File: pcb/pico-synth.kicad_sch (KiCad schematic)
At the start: 48 parts, among them J1 JST XH 2P, J2 JST XH 5P, J3 JST XH 4P, J4 JST XH 3P, SW1 Rotary_Encoder_Switch, U1 Pico, U2 6N137, U3 24LC512, U4 MCP4822, U5 LTC1044, U6 TL071, U7 TL072

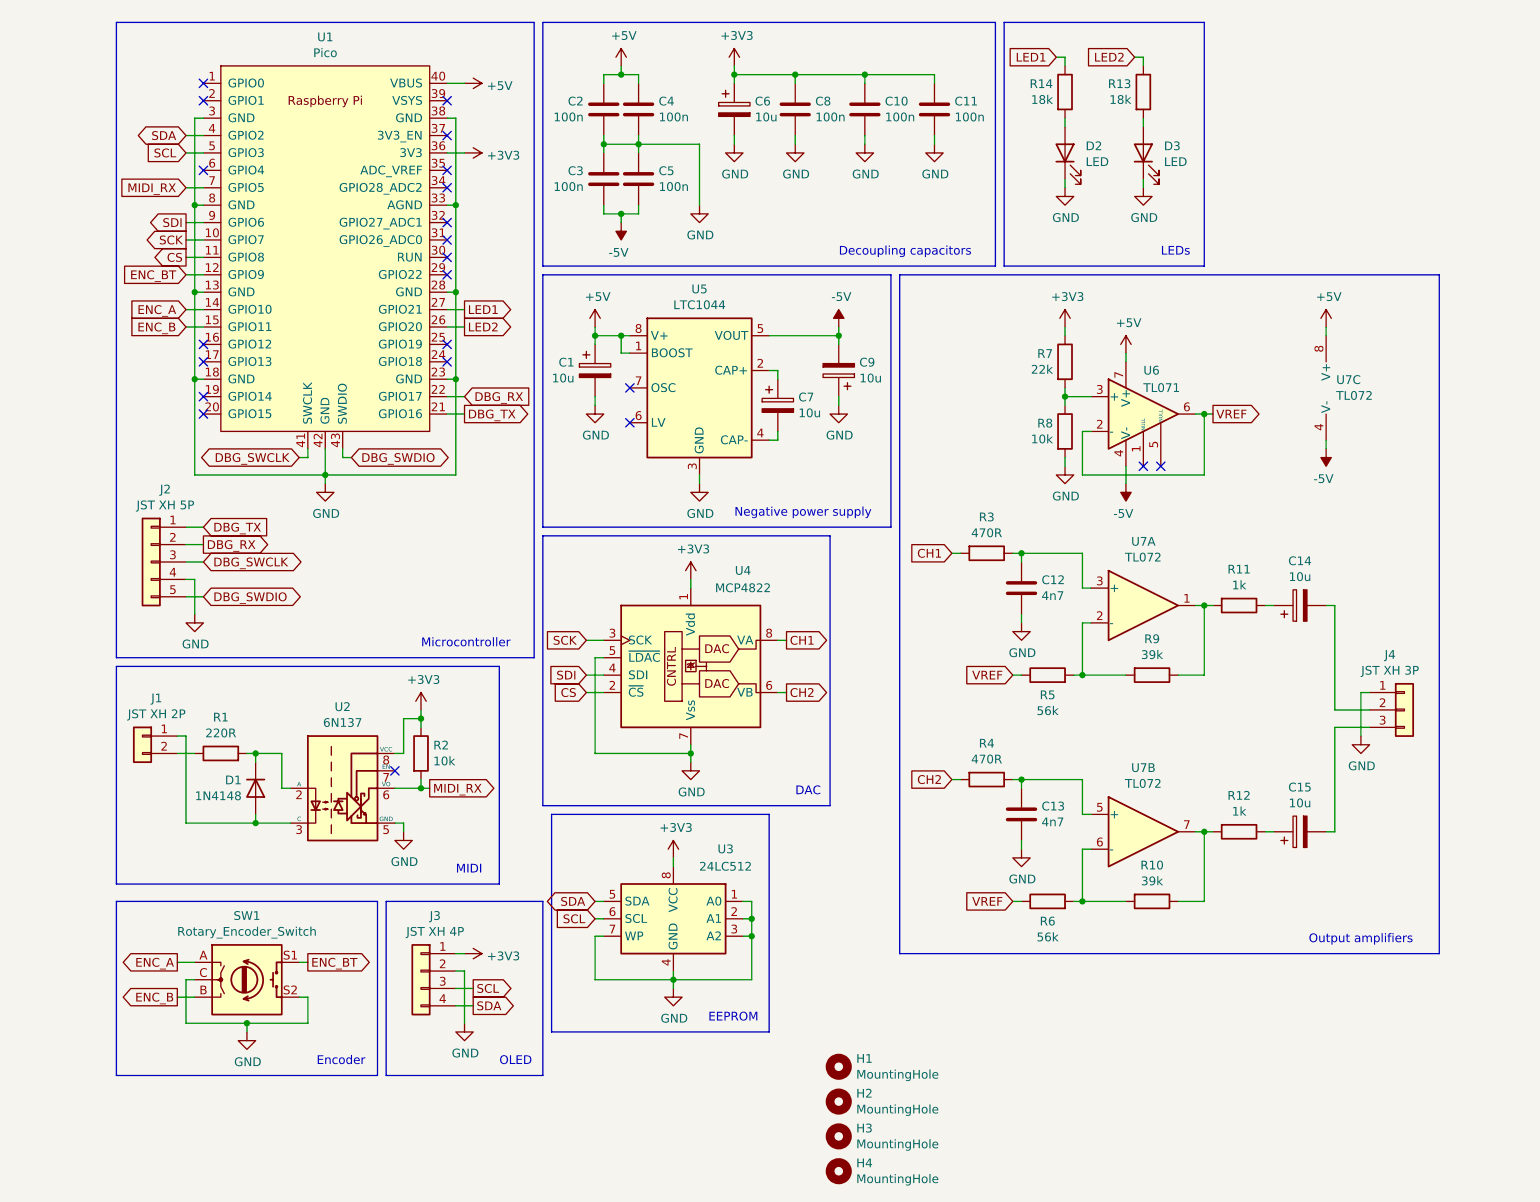
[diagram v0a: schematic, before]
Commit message: new hardware revision: 3.0
- added better output filter (Sallen-Key low pass filter)
- use MCP4822's LDAC pin to avoid (minimal, negligible :) phase drift
  between the channels
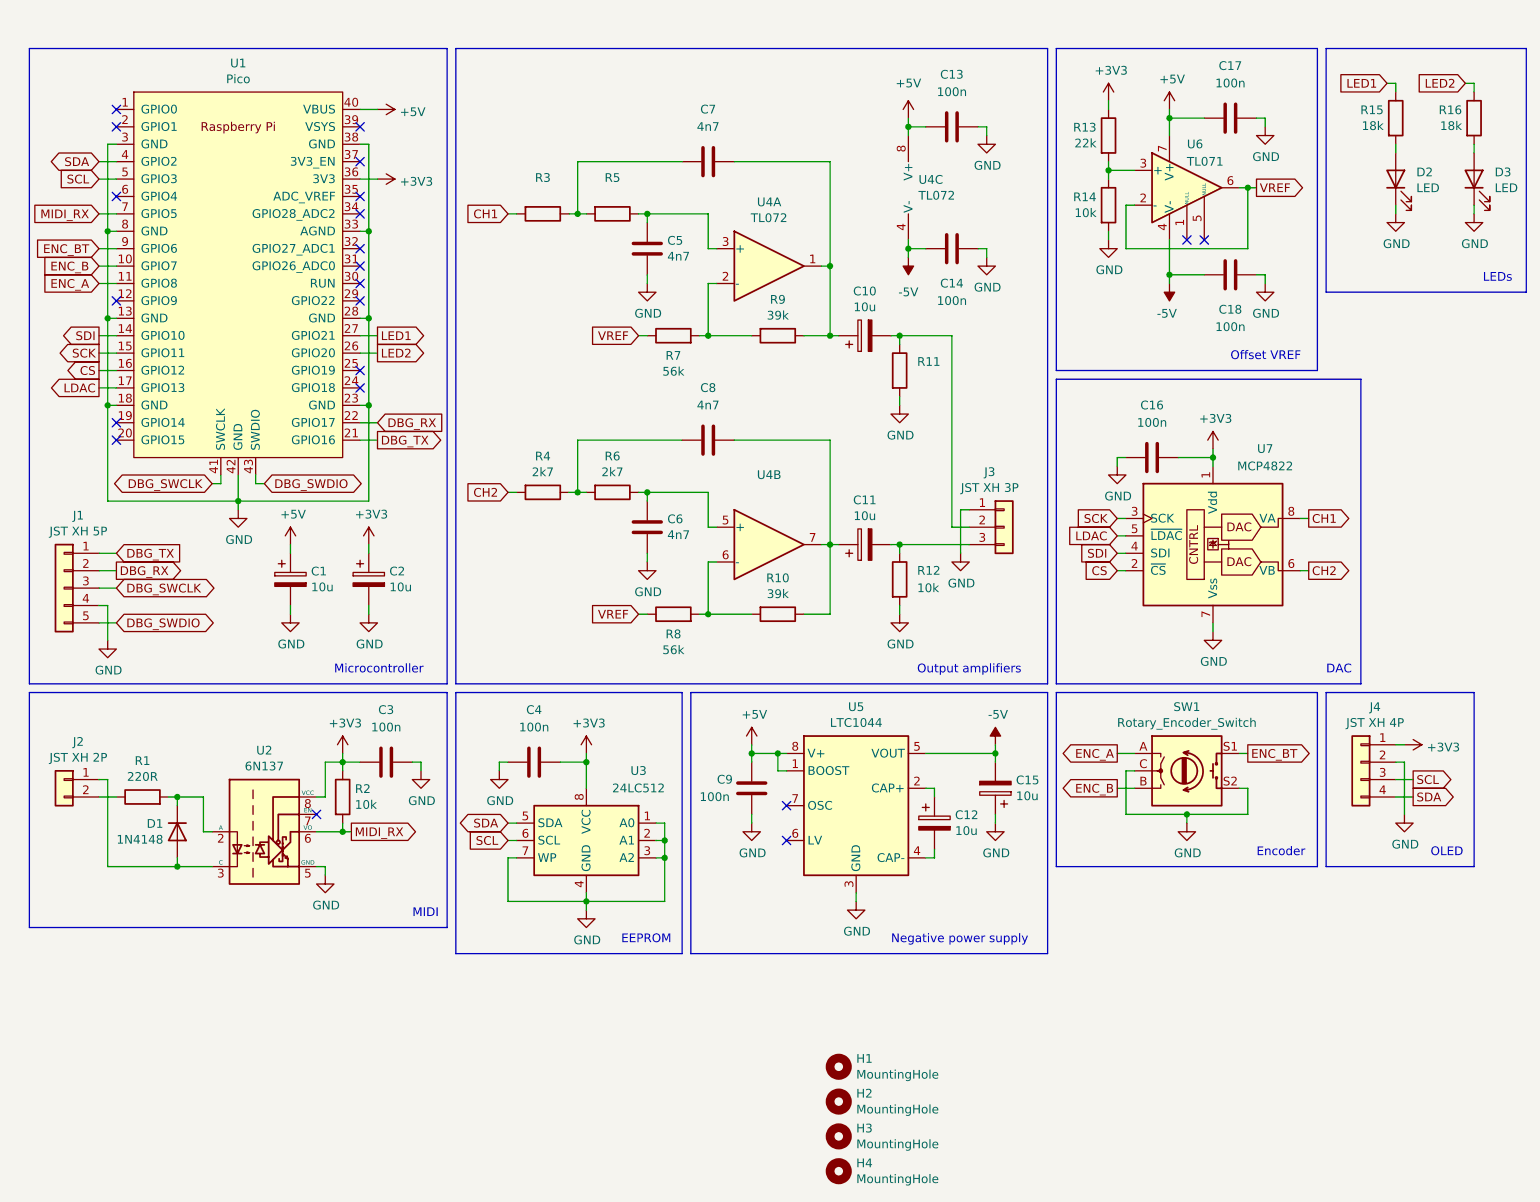
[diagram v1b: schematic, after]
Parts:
- removed C10, C11, C2, C5: 100n, Capacitor_THT:C_Disc_D4.3mm_W1.9mm_P5.00mm, symbol Device:C
- removed C15, C6: 10u, Capacitor_THT:CP_Radial_D5.0mm_P2.50mm, symbol Device:C_Polarized
- removed unit 2 of U7
- added C11, C2: 10u, Capacitor_THT:CP_Radial_D5.0mm_P2.50mm, symbol Device:C_Polarized
- added C14, C16, C17, C18, C9: 100n, Capacitor_THT:C_Disc_D4.3mm_W1.9mm_P5.00mm, symbol Device:C
- added C6, C7: 4n7, symbol Device:C
- added R3: (no value), Resistor_THT:R_Axial_DIN0207_L6.3mm_D2.5mm_P10.16mm_Horizontal, symbol Device:R
- added R8: 56k, Resistor_THT:R_Axial_DIN0207_L6.3mm_D2.5mm_P10.16mm_Horizontal, symbol Device:R
- added unit 2 of U4
- C13: value 4n7 -> 100n; footprint Capacitor_THT:C_Disc_D3.0mm_W1.6mm_P2.50mm -> Capacitor_THT:C_Disc_D4.3mm_W1.9mm_P5.00mm
- C5: renamed from C12; footprint Capacitor_THT:C_Disc_D3.0mm_W1.6mm_P2.50mm -> (none)
- C8: value 100n -> 4n7; footprint Capacitor_THT:C_Disc_D4.3mm_W1.9mm_P5.00mm -> (none)
- R11: value 1k -> (none)
- R12: value 1k -> 10k
- R4: value 470R -> 2k7
- R5: renamed from R3; value 470R -> (none)
- R6: value 56k -> 2k7
- U2: footprint (none) -> Package_DIP:DIP-8_W7.62mm_LongPads
- renumbered C14 to C10, C7 to C12, C9 to C15, J2 to J1, J1 to J2, J4 to J3, J3 to J4, R7 to R13, R8 to R14, R14 to R15, R13 to R16, R5 to R7, U7 to U4, U4 to U7
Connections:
- net +3V3: now also C3.1, C4.2, C16.2, C2.1; no longer C8.1
- net +5V: now also C13.1, C17.1, C9.1; no longer C4.1
- net -5V: now also C14.1, C18.1; no longer C3.2
- net CH1: now also R3.2; no longer R5.2
- net CS: now also U1.16 (GPIO12); no longer U1.11 (GPIO8)
- net ENC_A: now also U1.11 (GPIO8); no longer U1.14 (GPIO10)
- net ENC_B: now also U1.10 (GPIO7); no longer U1.15 (GPIO11)
- net ENC_BT: now also U1.9 (GPIO6); no longer U1.12 (GPIO9)
- net GND: now also C3.2, C4.1, R11.2, R12.2, C14.2, C16.1, C17.2, C18.2, C2.2, C6.2, C9.2; no longer C3.1, C4.2, C8.2, U7.5 (~{LDAC})
- net SCK: now also U1.15 (GPIO11); no longer U1.10 (GPIO7)
- net SDI: now also U1.14 (GPIO10); no longer U1.9 (GPIO6)
- net VREF: now also R8.1; no longer R6.1
- net at R9.1, U4.1: now also C10.1, C7.2; no longer R11.2
- net at R4.1: now also C8.1, R6.2; no longer C13.1
- net at R10.2: now also R8.2, U4.6 (-); no longer R6.2
- net at R10.1: now also C8.2, C11.1, U4.7; no longer R12.2
- net at R11.1: now also C10.2, J3.2 (Pin_2); no longer C10.1
- net at R12.1: now also J3.3 (Pin_3), C11.2
- net LDAC: now reaches U1.17 (GPIO13)
- net LDAC: now also U7.5 (~{LDAC})
- new net: C7.1, R3.1, R5.2
- new net: C6.1, R6.1, U4.5 (+)
- no-connect marks 22 -> 21
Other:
- note added: "Offset VREF"
- note removed: "Decoupling capacitors"
- moved on the sheet: C10, C12, C15, C5, D1, D2, D3, J1, J2, J3, J4, R1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

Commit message: pcb: new hardware revision: 4.0
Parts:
- removed C12, C15: 10u, Capacitor_THT:CP_Radial_D5.0mm_P2.50mm, symbol Device:C_Polarized
- removed C14, C17, C18, C9: 100n, Capacitor_THT:C_Disc_D4.3mm_W1.9mm_P5.00mm, symbol Device:C
- removed R13: 22k, Resistor_THT:R_Axial_DIN0207_L6.3mm_D2.5mm_P10.16mm_Horizontal, symbol Device:R
- removed R14: 10k, Resistor_THT:R_Axial_DIN0207_L6.3mm_D2.5mm_P10.16mm_Horizontal, symbol Device:R
- removed U5: LTC1044, Package_DIP:DIP-8_W7.62mm_LongPads, symbol Regulator_SwitchedCapacitor:LTC1044
- removed U6: TL071, Package_DIP:DIP-8_W7.62mm_LongPads, symbol Amplifier_Operational:TL071
- C5, C6: footprint (none) -> Capacitor_THT:C_Rect_L7.0mm_W2.5mm_P5.00mm
- C7, C8: value 4n7 -> (none); footprint (none) -> Capacitor_THT:C_Rect_L7.0mm_W2.5mm_P5.00mm
- R10, R9: value 39k -> (none)
- R11: value (none) -> 10k
- R4, R6: value 2k7 -> (none)
- U4: value TL072 -> (none)
- U4: footprint (none) -> Package_DIP:DIP-8_W7.62mm_LongPads
- renumbered C11 to C10, C13 to C11, C16 to C12, C10 to C9, J4 to J3, J3 to J4, R15 to R13, R16 to R14, U7 to U5
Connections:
- net -5V is gone; now on net GND: U4.4 (V-)
- net VREF is gone; now on net GND: R7.1, R8.1
- no-connect marks 21 -> 17
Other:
- note removed: "Negative power supply"
- note removed: "Offset VREF"
- moved on the sheet: C1, C10, C11, C12, C2, C3, C4, C5, C6, C7, C8, C9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

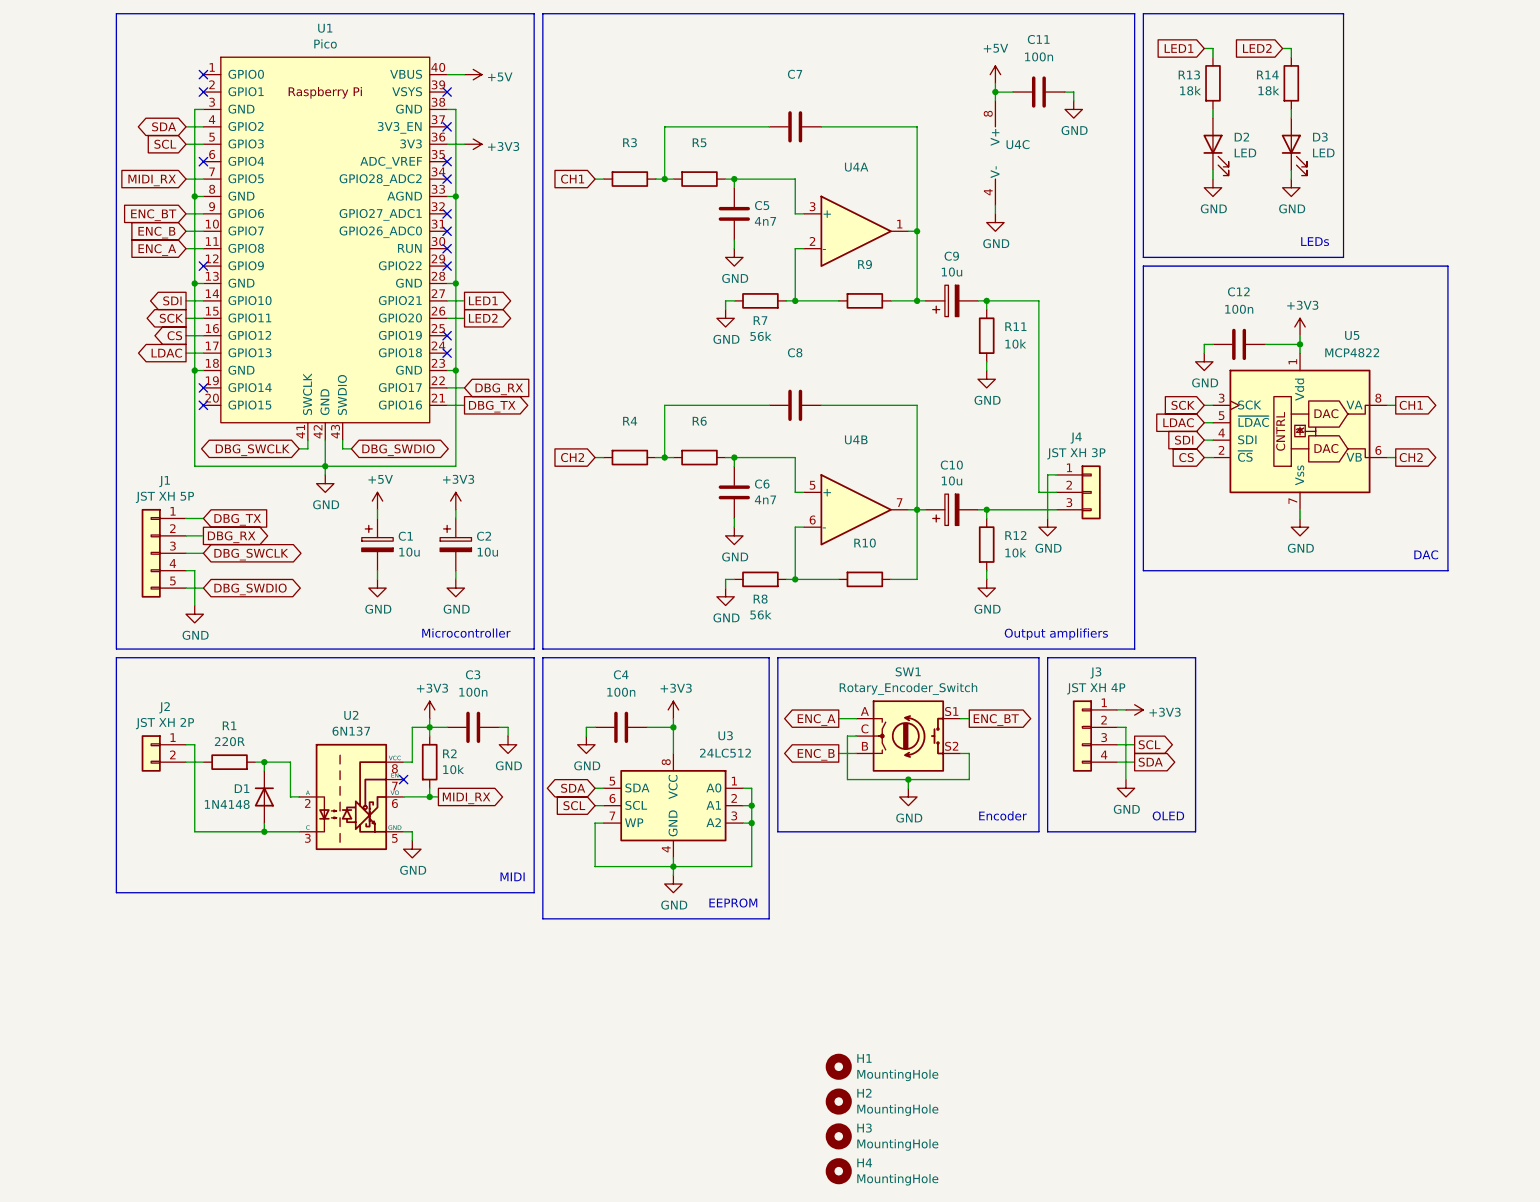
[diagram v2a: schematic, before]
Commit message: pcb: new hardware revision: 4.2
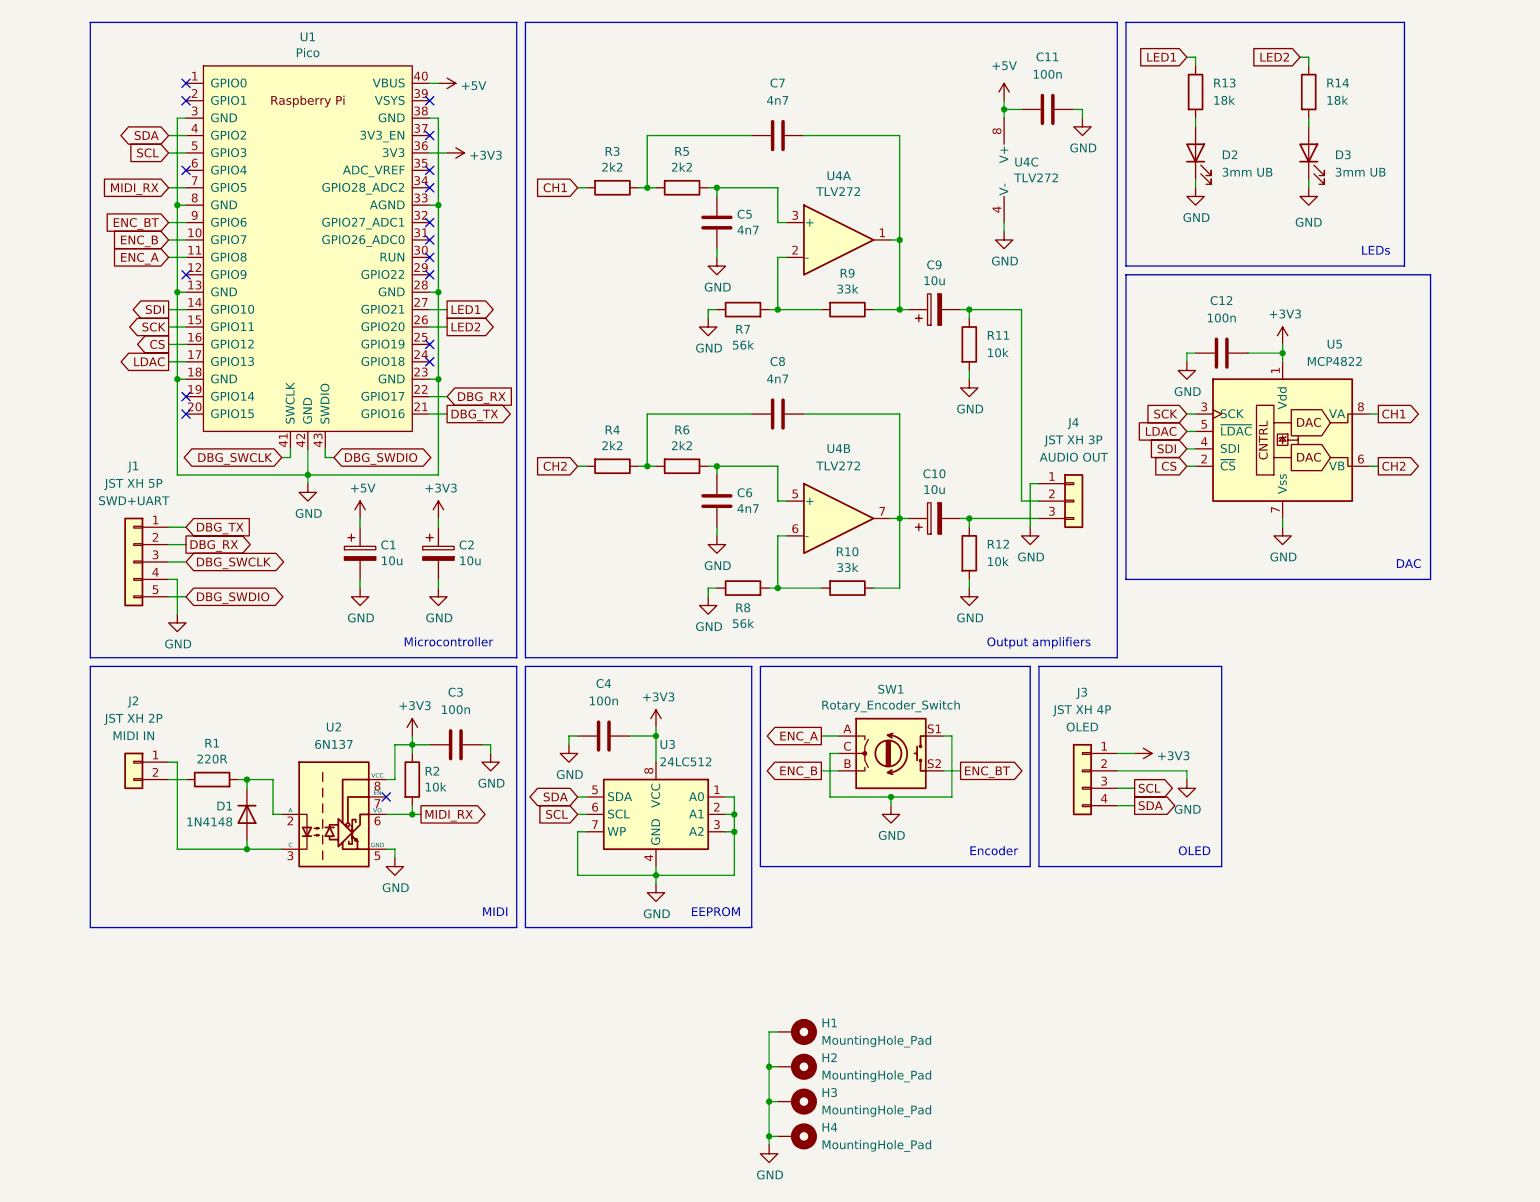
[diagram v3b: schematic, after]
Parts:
- removed H1, H2, H3, H4: MountingHole, MountingHole:MountingHole_2.2mm_M2_Pad_Via, symbol Mechanical:MountingHole
- added H1, H2, H3, H4: MountingHole_Pad, MountingHole:MountingHole_2.2mm_M2_Pad_Via, symbol Mechanical:MountingHole_Pad
- C7, C8: value (none) -> 4n7
- D2, D3: value LED -> 3mm UB
- J1: footprint Connector_JST:JST_XH_B5B-XH-A_1x05_P2.50mm_Vertical -> Connector_JST_with_PinSocket:JST_XH_B5B-XH-A_PinSocket_1x05_P2.50mm_Vertical
- J2: footprint Connector_JST:JST_XH_B2B-XH-A_1x02_P2.50mm_Vertical -> Connector_JST_with_PinSocket:JST_XH_B2B-XH-A_PinSocket_1x02_P2.50mm_Vertical
- J3: footprint Connector_JST:JST_XH_B4B-XH-A_1x04_P2.50mm_Vertical -> Connector_JST_with_PinSocket:JST_XH_B4B-XH-A_PinSocket_1x04_P2.50mm_Vertical
- J4: footprint Connector_JST:JST_XH_B3B-XH-A_1x03_P2.50mm_Vertical -> Connector_JST_with_PinSocket:JST_XH_B3B-XH-A_PinSocket_1x03_P2.50mm_Vertical
- R10, R9: value (none) -> 33k
- R3, R4, R5, R6: value (none) -> 2k2
- U2, U3, U5: footprint Package_DIP:DIP-8_W7.62mm_LongPads -> Package_DIP:DIP-8_W7.62mm
- U4: value (none) -> TLV272; footprint Package_DIP:DIP-8_W7.62mm_LongPads -> Package_DIP:DIP-8_W7.62mm; symbol Amplifier_Operational:TL072 -> TLV272:TLV272
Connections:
- net ENC_BT: now also SW1.S2; no longer SW1.S1
- net GND: now also SW1.S1, H1.1, H2.1, H3.1, H4.1; no longer SW1.S2
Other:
- moved on the sheet: C1, C10, C11, C12, C2, C3, C4, C5, C6, C7, C8, C9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
